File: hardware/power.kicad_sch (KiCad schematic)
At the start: 8 parts, among them U4 NCP565D2T33R4G, U6 SPBW06F-05

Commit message: Fixes after review
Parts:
- removed C1: C_Polarized, electrolytic_cap:EEE0GA101SR, symbol Device:C_Polarized
- added C20, C21: 10u, 10uCap:CAPC3225X280N, symbol Device:C_Small
- added C22, C23: 22uF, Capacitor_SMD:CP_Elec_4x5.8, symbol Device:C_Polarized_Small
- added C25: 47u, 47uCapPolarized:EEE1AA220WR, symbol Device:C_Polarized_Small
- added D10: 30V, Diode_SMD:D_SOD-123, symbol Device:D_Zener_Small
- added D5: LED, symbol Device:LED
- added D9: 10V, Diode_SMD:D_SOD-123, symbol Device:D_Zener_Small
- added F1: 250mA, 24V250mAFuse:FUSC1608X43N, symbol Device:Fuse_Small
- added Q1: SI2347DS-T1-GE3, Package_TO_SOT_SMD:SOT-23-3, symbol Transistor_FET:Q_PMOS_GSD
- added R12: 220R, symbol Device:R
- added R15: 100k, Resistor_SMD:R_0603_1608Metric_Pad0.98x0.95mm_HandSolder, symbol Device:R_Small
- C2, C3: value 150pF -> 150pF X2/Y3; Mouser https://www.mouser.pl/ProductDetail/Vishay/VJ1206A151JXFTW1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 -> https://www.mouser.pl/ProductDetail/Knowles-Novacap/LS1808N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
- L1: value L -> 10u
- U6: Mouser Price/Stock https://www.mouser.pl/ProductDetail/MEAN-WELL/SPBW03F-05?qs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 -> https://www.mouser.pl/ProductDetail/MEAN-WELL/SPBW06F-05?qs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
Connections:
- net +24V: now also F1.1; no longer L1.1
- net +3.3V: now also R12.2
- net +5V: now also C25.1
- net GND: now also C25.2, D5.1 (K)
- net GND_EXT: now also C20.2, C21.2, C22.2, C23.2, D10.2 (A), R15.2
- new net: C20.1, C21.1, C22.1, C23.1, D9.1 (K), L1.1, Q1.2 (S)
- new net: D9.2 (A), Q1.1 (G), R15.1
- new net: D10.1 (K), F1.2, Q1.3 (D)
- new net: D5.2 (A), R12.1
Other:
- moved on the sheet: C2, U6

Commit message: Added pi-filter to VANT and added socket for battery
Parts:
- C20, C21: Mouser (none) -> https://www.mouser.pl/ProductDetail/Samsung-Electro-Mechani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

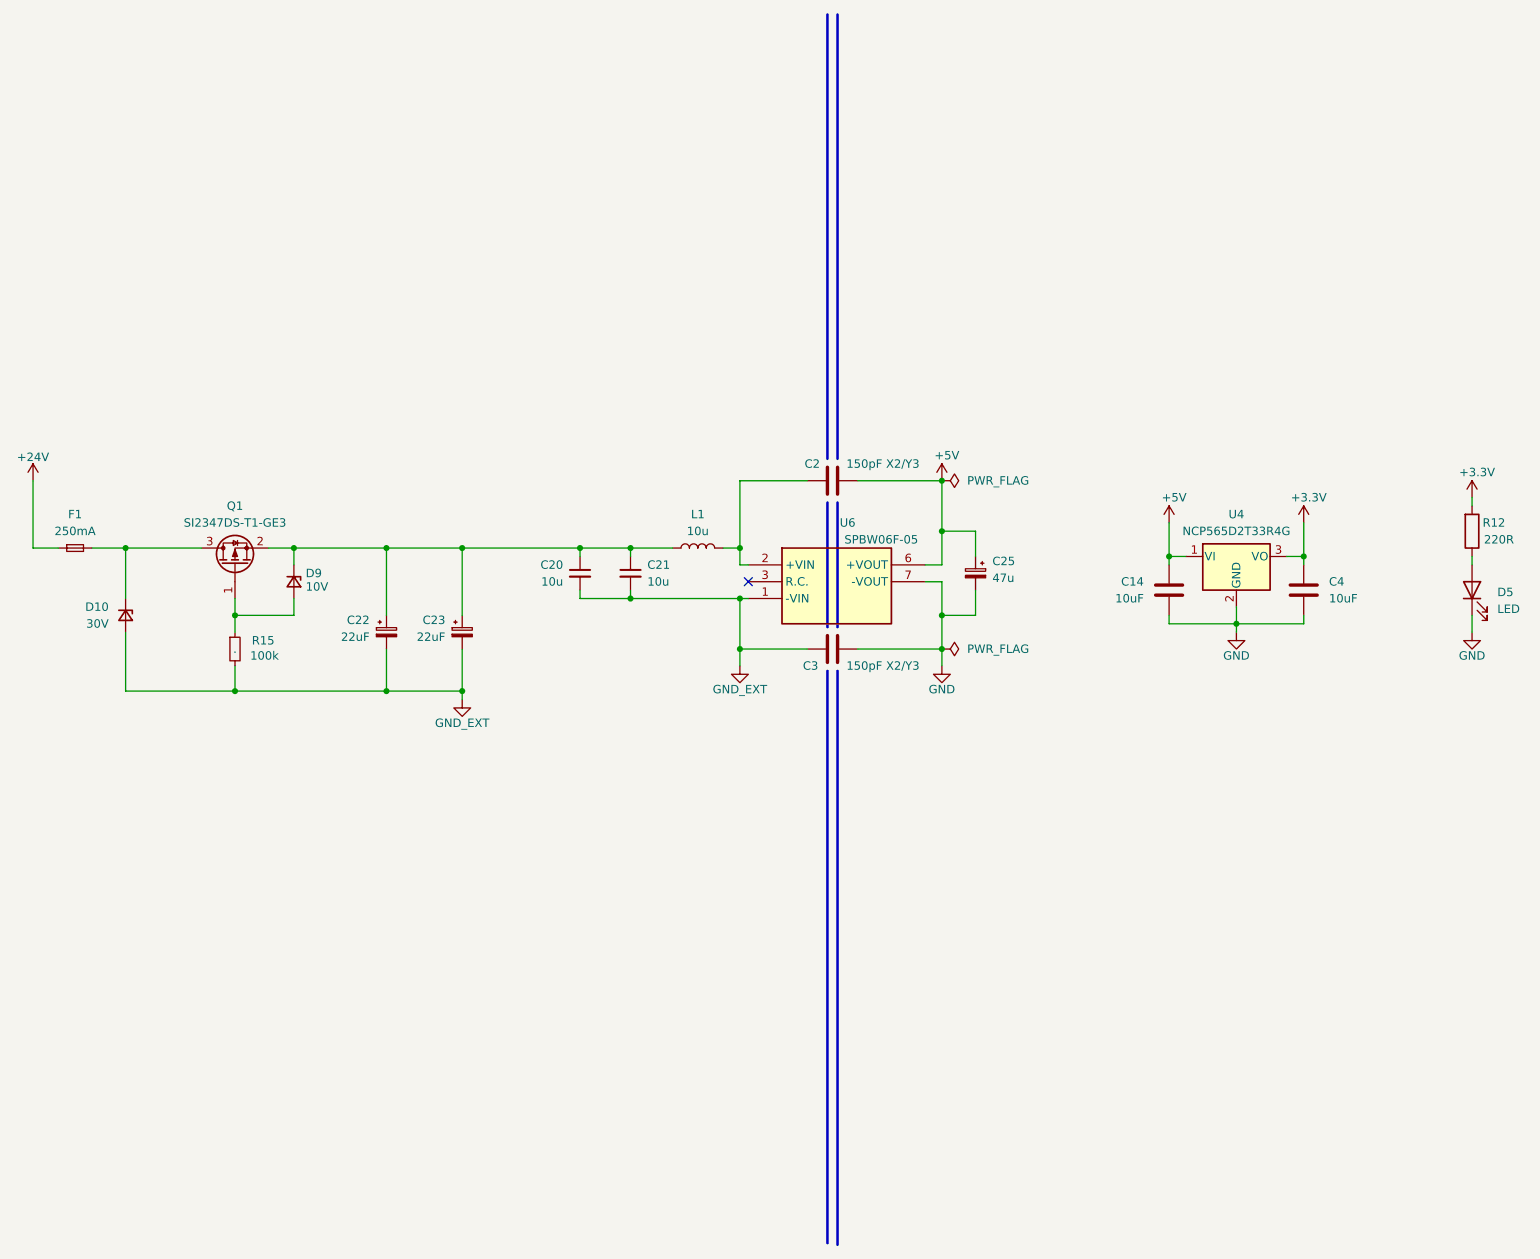
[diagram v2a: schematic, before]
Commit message: Fixes after review and mouser links for most components added
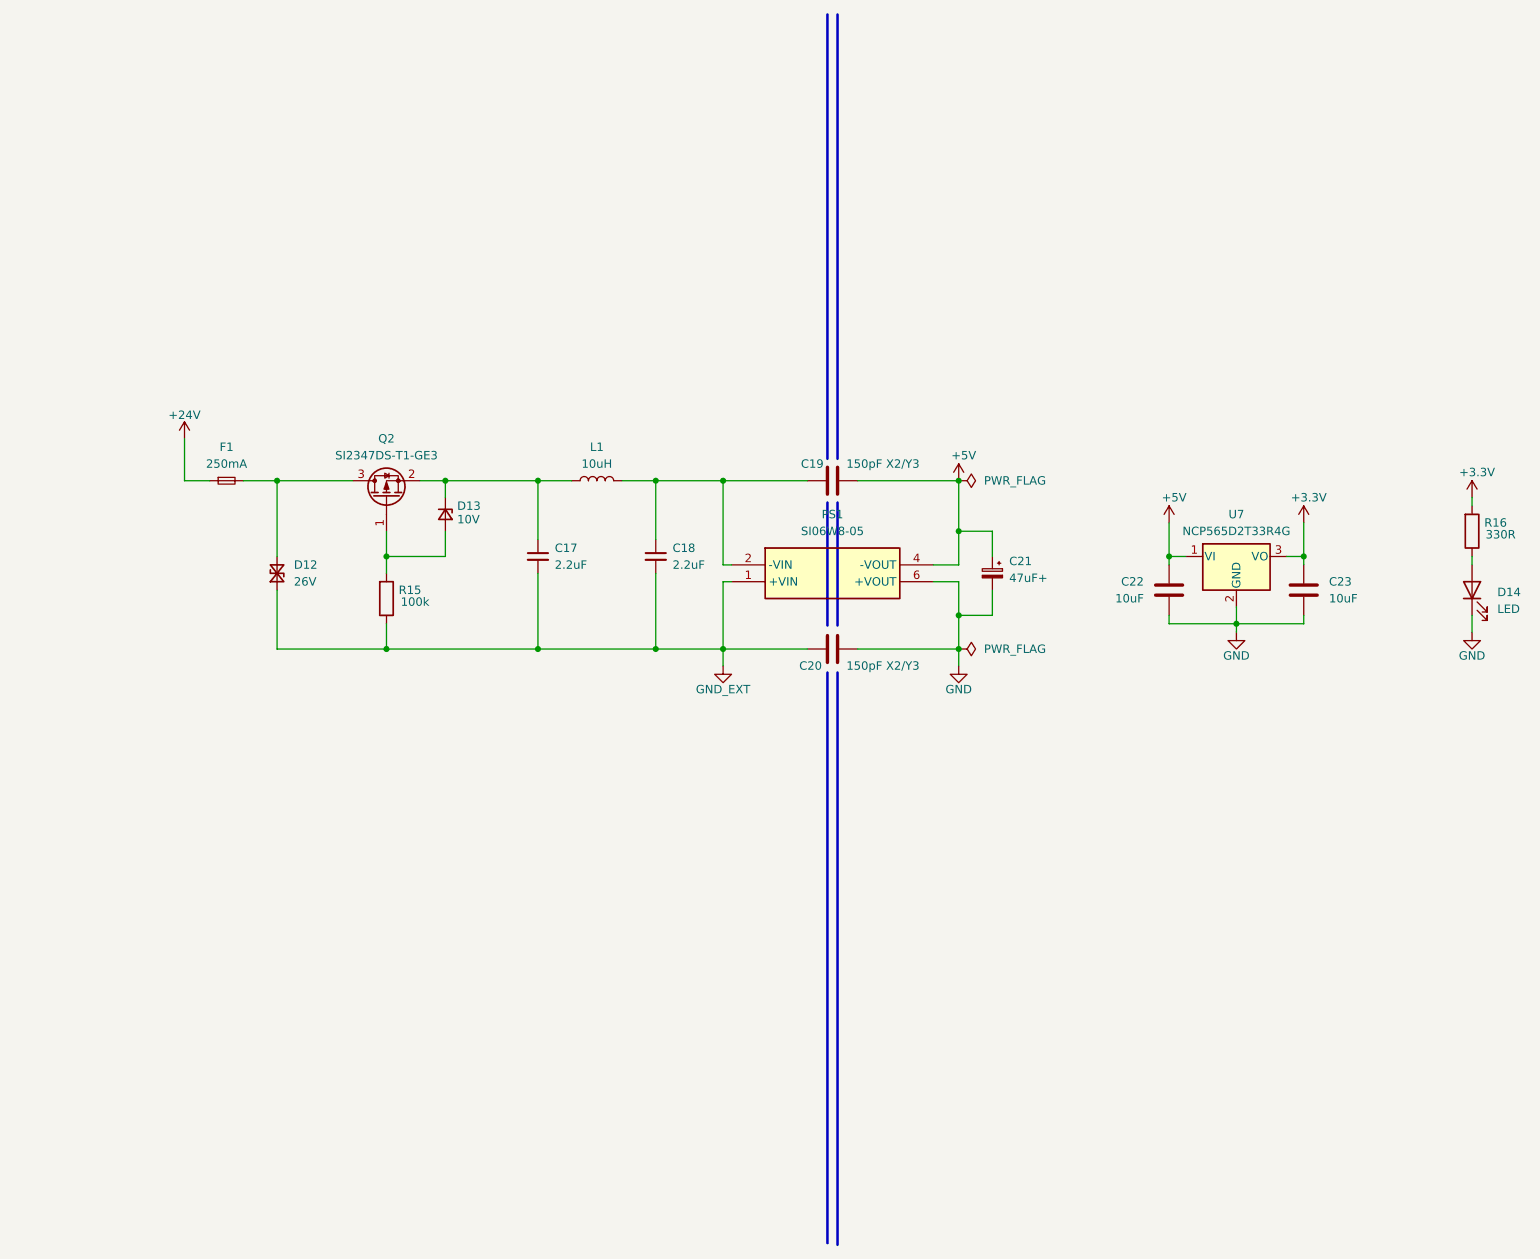
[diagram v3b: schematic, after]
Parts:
- removed C21: 10u, 10uCap:CAPC3225X280N, symbol Device:C_Small
- removed C22, C23: 22uF, Capacitor_SMD:CP_Elec_4x5.8, symbol Device:C_Polarized_Small
- removed C4: 10uF, symbol Device:C
- removed D10: 30V, Diode_SMD:D_SOD-123, symbol Device:D_Zener_Small
- removed R15: 100k, Resistor_SMD:R_0603_1608Metric_Pad0.98x0.95mm_HandSolder, symbol Device:R_Small
- removed U6: SPBW06F-05, DCisoconv:SPBW06F05, symbol spbw06f-05:SPBW06F-05
- added C18: 2.2uF, Capacitor_SMD:C_1206_3216Metric_Pad1.33x1.80mm_HandSolder, symbol Device:C_Small
- added C23: 10uF, Capacitor_SMD:C_0603_1608Metric_Pad1.08x0.95mm_HandSolder, symbol Device:C
- added D12: 26V, symbol Device:D_TVS_Small
- added PS1: SI06W8-05, SI06W805, symbol SI06W8-05:SI06W8-05
- added R15: 100k, Resistor_SMD:R_0603_1608Metric_Pad0.98x0.95mm_HandSolder, symbol Device:R
- C17: renamed from C20; value 10u -> 2.2uF; footprint 10uCap:CAPC3225X280N -> Capacitor_SMD:C_1206_3216Metric_Pad1.33x1.80mm_HandSolder; Mouser https://www.mouser.pl/ProductDetail/Samsung-Electro-Mechani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 -> https://www.mouser.pl/ProductDetail/Murata-Electronics/GRM3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
- C19: renamed from C2; footprint (none) -> 150pFCaps:CAPC4620X165N
- C20: renamed from C3; footprint (none) -> 150pFCaps:CAPC4620X165N
- C21: renamed from C25; value 47u -> 47uF+
- C22: renamed from C14; footprint (none) -> Capacitor_SMD:C_0603_1608Metric_Pad1.08x0.95mm_HandSolder; Mouser (none) -> https://www.mouser.pl/ProductDetail/Murata-Electronics/GRM1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
- L1: value 10u -> 10uH
- Q2: renamed from Q1; Mouser (none) -> https://www.mouser.pl/ProductDetail/Vishay-Siliconix/SI2347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
- R16: renamed from R12; value 220R -> 330R; footprint (none) -> Resistor_SMD:R_0603_1608Metric_Pad0.98x0.95mm_HandSolder; Mouser (none) -> https://www.mouser.pl/ProductDetail/Vishay-Draloric/RCS0603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
- renumbered D9 to D13, D5 to D14, U4 to U7
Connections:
- net +3.3V: now also C23.2
- net +5V: now also PS1.4 (-VOUT)
- net GND: now also C23.1, PS1.6 (+VOUT)
- net GND_EXT: now also C18.2, D12.1 (A1), PS1.1 (+VIN), R15.1
- net at C19.1, L1.2: now also C18.1, PS1.2 (-VIN)
- net at D13.2 (A), Q2.1 (G): now also R15.2
- net at F1.2, Q2.3 (D): now also D12.2 (A2)
- no-connect marks 1 -> 0
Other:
- moved on the sheet: C17, C21, D13, F1, L1, Q2

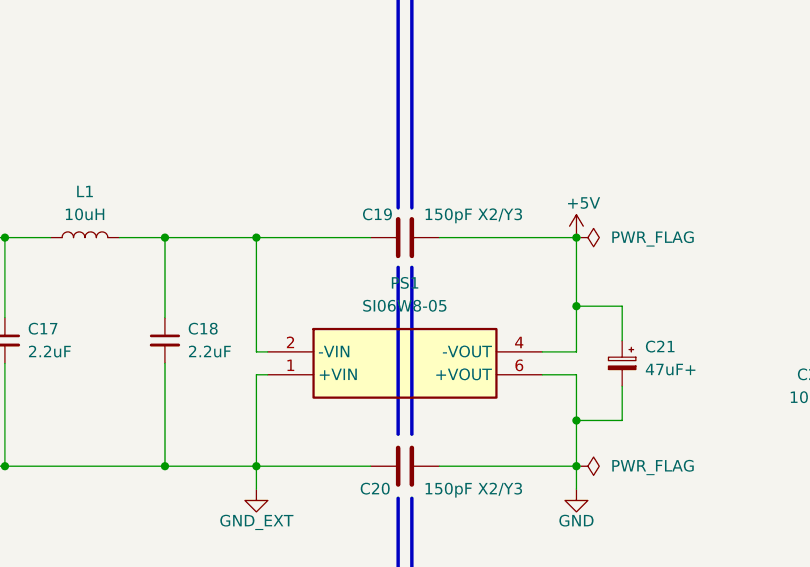
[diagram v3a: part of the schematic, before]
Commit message: changed some elements on shematic
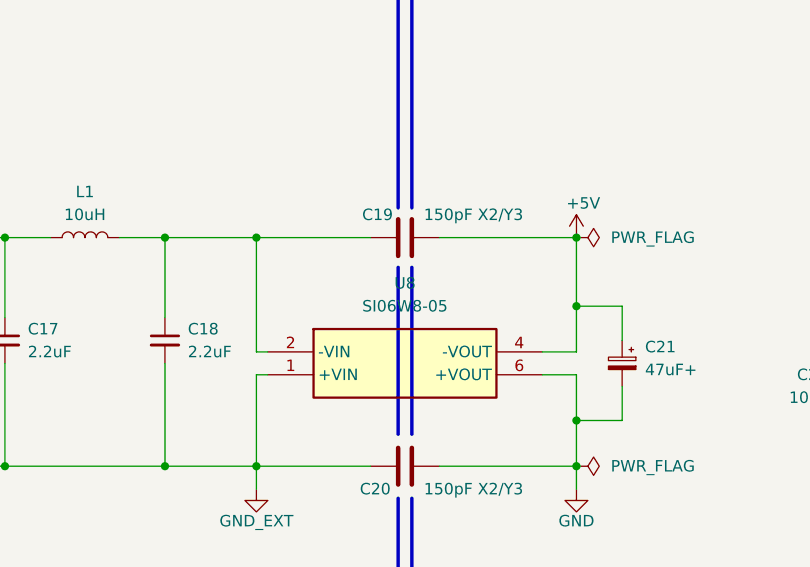
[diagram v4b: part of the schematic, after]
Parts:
- D12: footprint (none) -> 24VinputTVS:SMFA2005CA
- D13: footprint Diode_SMD:D_SOD-123 -> Zener10V:SOD3716X135N; Mouser (none) -> https://www.mouser.pl/ProductDetail/onsemi/SZMMSZ4697T1G?qs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; Mouser Part Number 863-MMSZ5240BT1G -> (none)
- D14: footprint (none) -> Diode_SMD:D_0603_1608Metric_Pad1.05x0.95mm_HandSolder; Mouser (none) -> https://www.mouser.pl/ProductDetail/Wurth-Elektronik/150060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
- U8: renamed from PS1; Mouser (none) -> https://www.mouser.pl/ProductDetail/MEAN-WELL/SI06W8-05?qs=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

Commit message: mistake correction
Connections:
- net +24V renamed +24V_EXT
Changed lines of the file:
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@@
 			)
 		)
-		(property "Value" "+24V"
+		(property "Value" "+24V_EXT"
 			(at 52.07 72.644 0)
 			(show_name no)

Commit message: 3D models, optocoupler added, pcb settings and components placing
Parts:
- U8: footprint SI06W805 -> DCisoconv:SI06W805

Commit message: All components placed on pcb
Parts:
- U7: footprint Package_TO_SOT_SMD:TO-263-2 -> 5VLDO3V3:TO-263-2
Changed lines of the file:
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@@
 			)
 		)
-		(property "Footprint" "Package_TO_SOT_SMD:TO-263-2"
+		(property "Footprint" "5VLDO3V3:TO-263-2"
 			(at 208.28 90.17 0)
 			(hide yes)

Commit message: Finished pcb routing
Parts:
- U8: Mouser Part Number https://www.mouser.pl/ProductDetail/MEAN-WELL/SI06W8-05?qs=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 -> (none)
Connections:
- net +5V: now also U8.6 (+VOUT); no longer U8.4 (-VOUT)
- net GND: now also U8.4 (-VOUT); no longer U8.6 (+VOUT)
- net GND_EXT: now also U8.2 (-VIN); no longer U8.1 (+VIN)
- net at C18.1, C19.1, L1.2: now also U8.1 (+VIN); no longer U8.2 (-VIN)
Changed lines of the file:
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@@
 	(wire
 		(pts
+			(xy 165.1 95.25) (xy 168.91 95.25)
+		)
+		(stroke
+			(width 0)
+			(type default)
+		)
+	)
+	(wire
+		(pts
 			(xy 168.91 97.79) (xy 168.91 102.87)
 		)
@@
 	(wire
 		(pts
-			(xy 133.35 95.25) (xy 134.62 95.25)
-		)
-		(stroke
-			(width 0)
-			(type default)
-		)
-	)
-	(wire
-		(pts
 			(xy 123.19 107.95) (xy 133.35 107.95)
 		)
@@
 	(wire
 		(pts
+			(xy 133.35 95.25) (xy 134.62 95.25)
+		)
+		(stroke
+			(width 0)
+			(type default)
+		)
+	)
+	(wire
+		(pts
 			(xy 200.66 93.98) (xy 200.66 95.25)
 		)
@@
 	(wire
 		(pts
-			(xy 165.1 95.25) (xy 168.91 95.25)
-		)
-		(stroke
-			(width 0)
-			(type default)
-		)
-	)
-	(wire
-		(pts
 			(xy 134.62 97.79) (xy 133.35 97.79)
 		)
@@
 	(symbol
 		(lib_id "SI06W8-05:SI06W8-05")
-		(at 134.62 95.25 0)
+		(at 134.62 97.79 0)
+		(mirror x)
 		(unit 1)
 		(body_style 1)
@@
 		(in_pos_files yes)
 		(dnp no)
-		(fields_autoplaced yes)
 		(property "Reference" "U8"
-			(at 149.86 87.63 0)
+			(at 153.924 89.154 0)
 			(show_name no)
 			(do_not_autoplace no)
@@
 		)
 		(property "Value" "SI06W8-05"
-			(at 149.86 90.17 0)
+			(at 156.464 91.44 0)
 			(show_name no)
 			(do_not_autoplace no)
@@
 		)
 		(property "Footprint" "DCisoconv:SI06W805"
-			(at 161.29 190.17 0)
+			(at 161.29 2.87 0)
 			(hide yes)
 			(show_name no)
@@
 		)
 		(property "Datasheet" "https://www.meanwell.com/upload/pdf/DI06W8/SI06W8,DI06W8-spec.pdf"
-			(at 161.29 290.17 0)
+			(at 161.29 -97.13 0)
 			(hide yes)
 			(show_name no)
@@
 		)
 		(property "Description" "Isolated DC/DC Converters - Through Hole 6W 9-75Vin 5V 0-1200mA 1x1 Regulated DIP"
-			(at 134.62 95.25 0)
-			(hide yes)
-			(show_name no)
-			(do_not_autoplace no)
-			(effects
-				(font
-					(size 1.27 1.27)
-				)
-			)
-		)
-		(property "Mouser Part Number" "https://www.mouser.pl/ProductDetail/MEAN-WELL/SI06W8-05?qs=ST9lo4GX8V3OoQwDIibogw%3D%3D"
-			(at 161.29 590.17 0)
-			(hide yes)
-			(show_name no)
-			(do_not_autoplace no)
-			(effects
-				(font
-					(size 1.27 1.27)
-				)
-				(justify left top)
-			)
-		)
-		(property "Author" ""
-			(at 134.62 95.25 0)
-			(hide yes)
-			(show_name no)
-			(do_not_autoplace no)
-			(effects
-				(font
-					(size 1.27 1.27)
-				)
-			)
-		)
-		(property "License" ""
-			(at 134.62 95.25 0)
-			(hide yes)
-			(show_name no)
-			(do_not_autoplace no)
-			(effects
-				(font
-					(size 1.27 1.27)
-				)
-			)
-		)
-		(property "MPN" ""
-			(at 134.62 95.25 0)
-			(hide yes)
-			(show_name no)
-			(do_not_autoplace no)
-			(effects
-				(font
-					(size 1.27 1.27)
-				)
-			)
-		)
-		(property "Manufacturer" ""
-			(at 134.62 95.25 0)
+			(at 134.62 97.79 0)
 			(hide yes)
 			(show_name no)
@@
 		)
 		(property "Mouser" "https://www.mouser.pl/ProductDetail/MEAN-WELL/SI06W8-05?qs=ST9lo4GX8V3OoQwDIibogw%3D%3D"
-			(at 134.62 95.25 0)
-			(hide yes)
-			(show_name no)
-			(do_not_autoplace no)
-			(effects
-				(font
-					(size 1.27 1.27)
-				)
-			)
-		)
-		(property "Sim.Device" ""
-			(at 134.62 95.25 0)
-			(hide yes)
-			(show_name no)
-			(do_not_autoplace no)
-			(effects
-				(font
-					(size 1.27 1.27)
-				)
-			)
-		)
-		(property "Sim.Type" ""
-			(at 134.62 95.25 0)
+			(at 134.62 97.79 0)
 			(hide yes)
 			(show_name no)
